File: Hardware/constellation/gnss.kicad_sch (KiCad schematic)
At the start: 0 parts

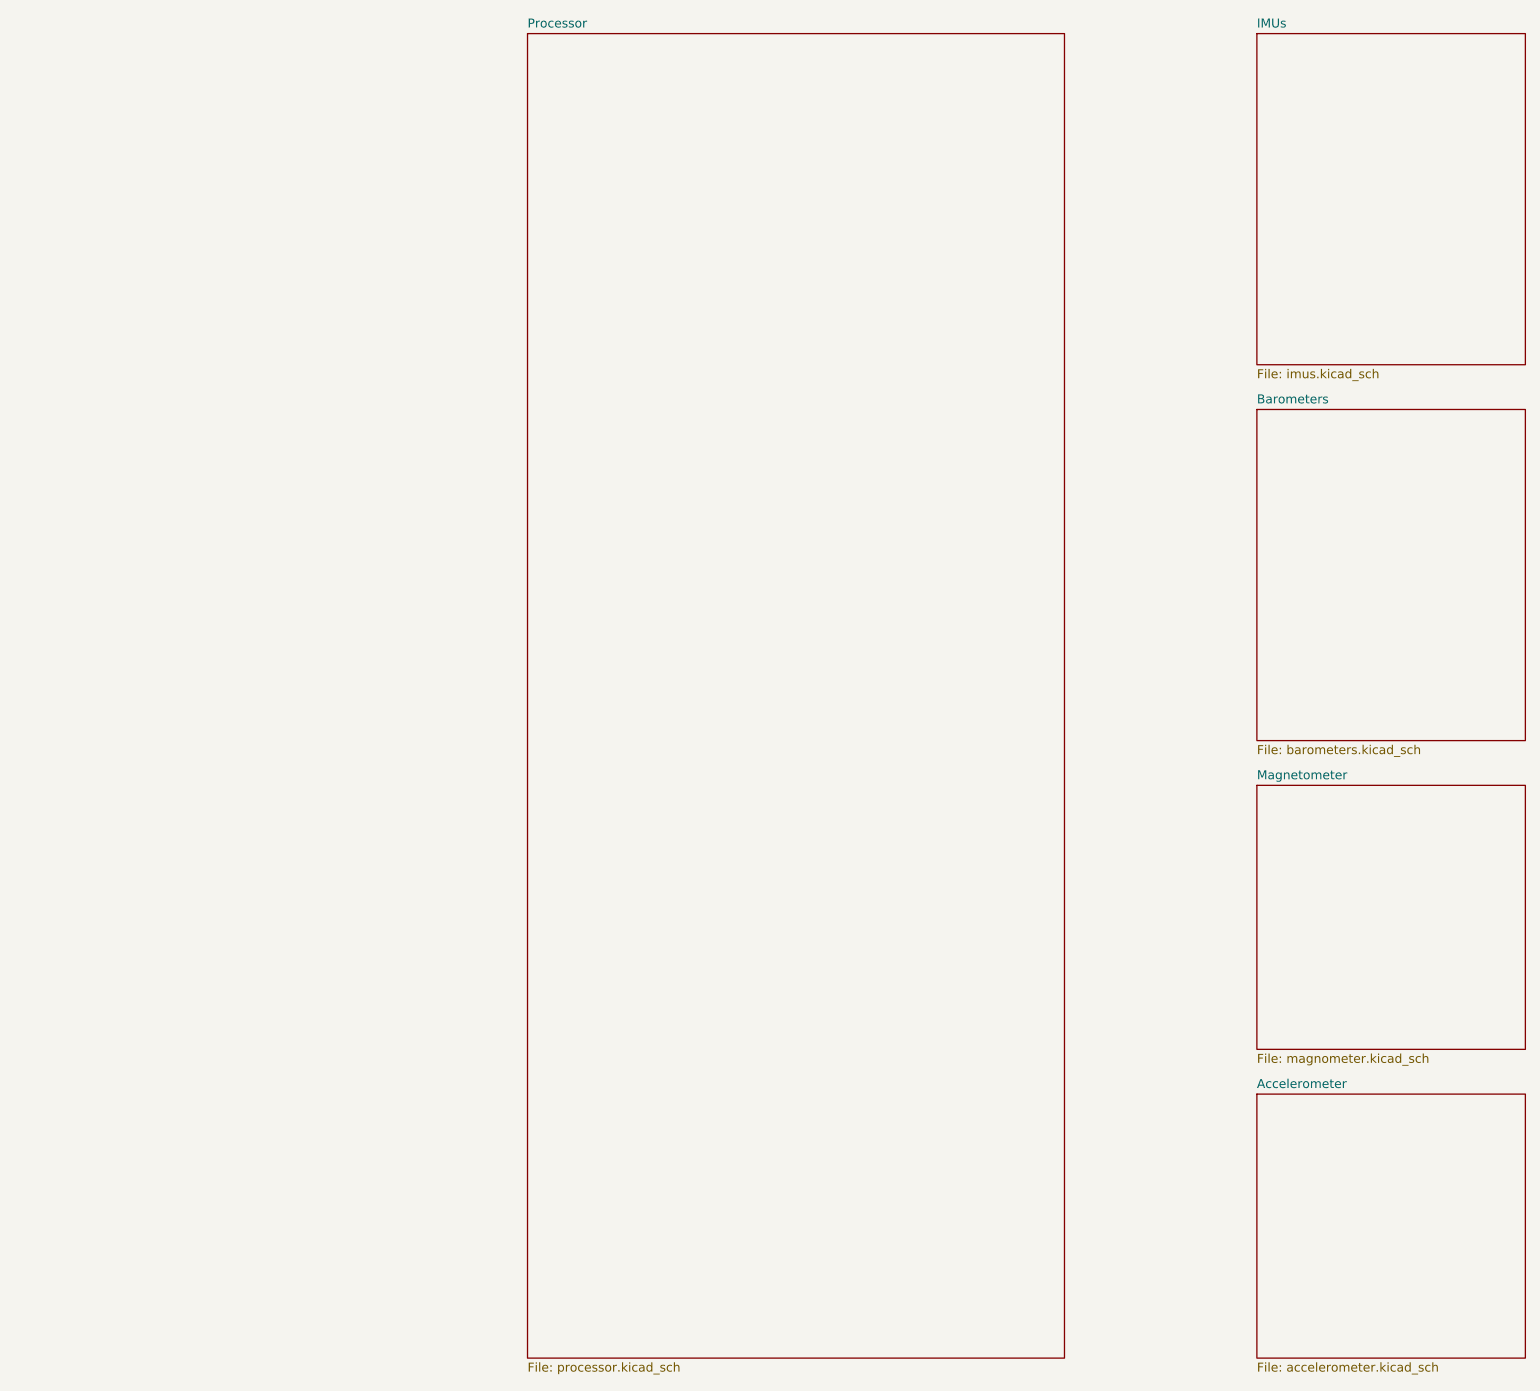
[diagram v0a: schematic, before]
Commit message: shift to hierarchial design, add GNSS, mag, accel
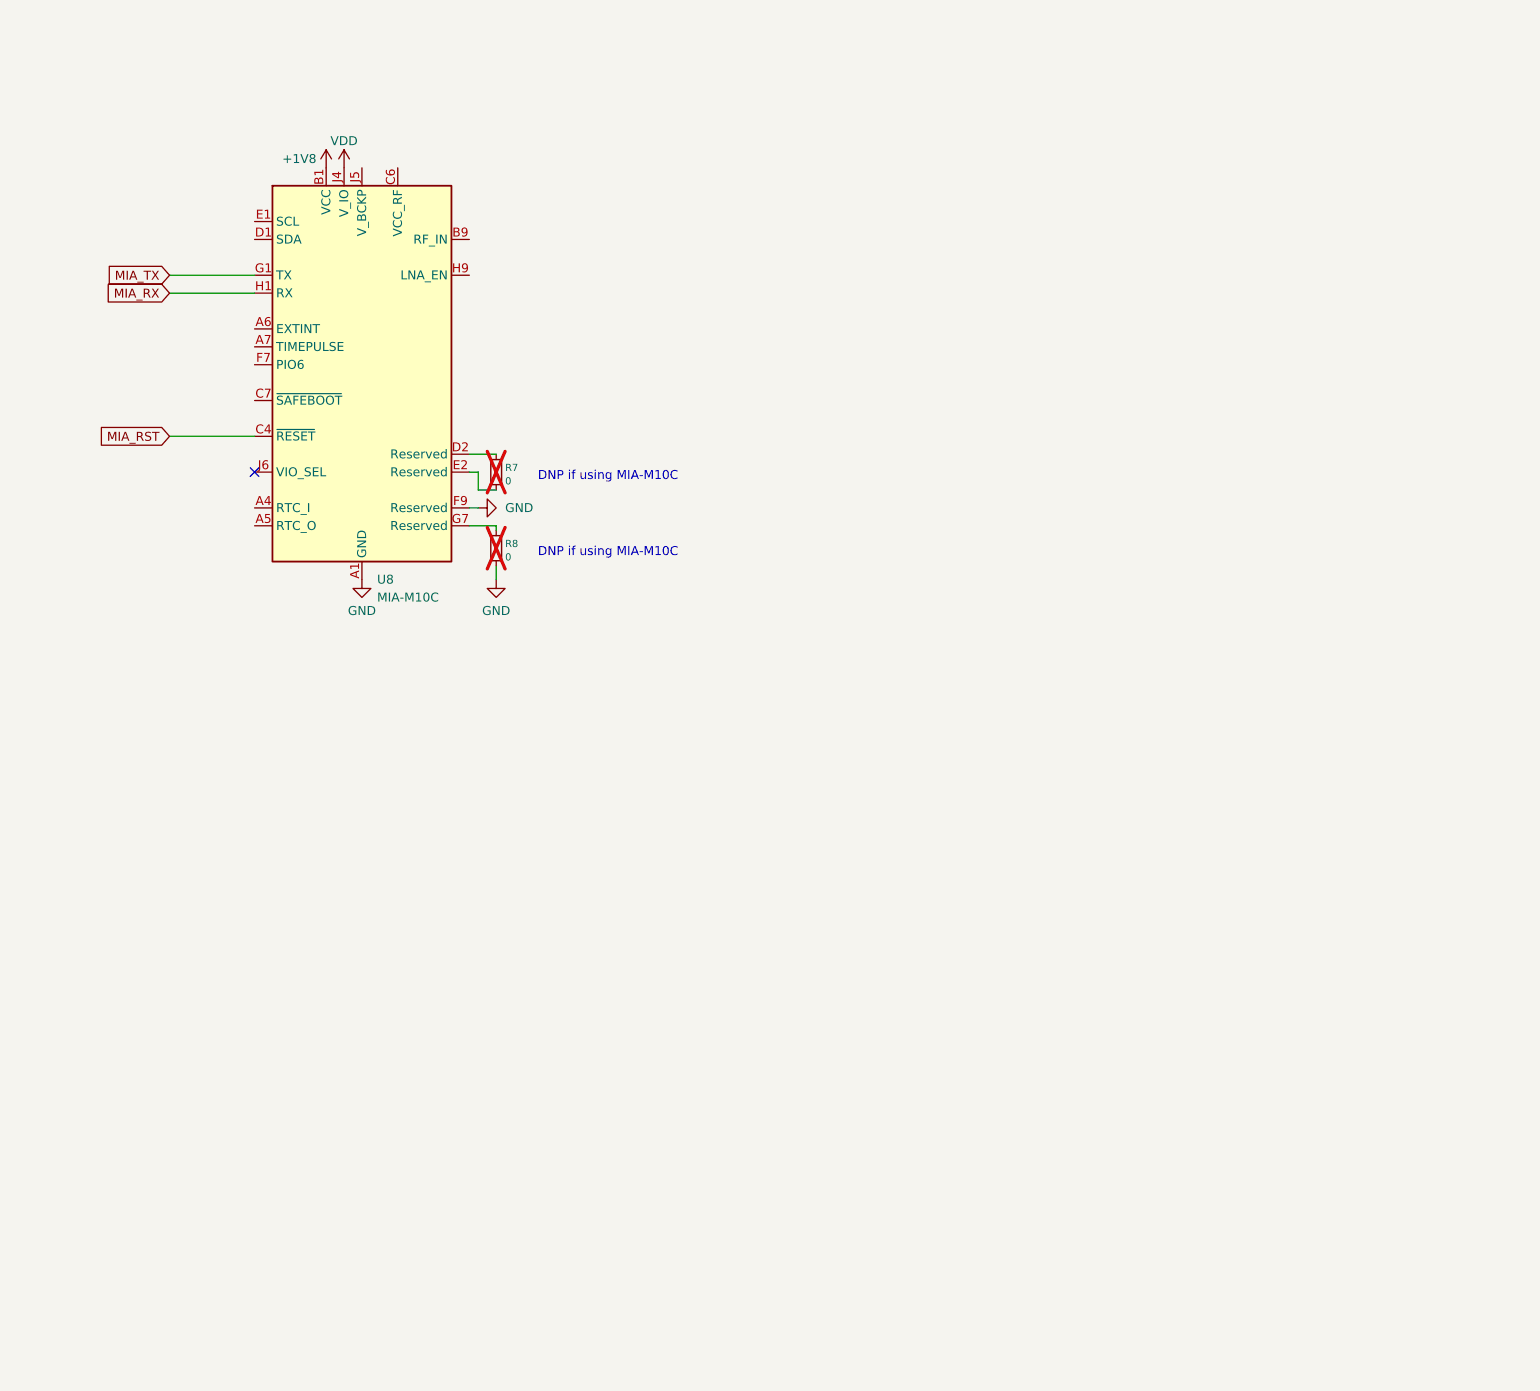
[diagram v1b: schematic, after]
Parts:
- added R7, R8: 0, Resistor_SMD:R_0402_1005Metric_Pad0.72x0.64mm_HandSolder, symbol Device:R_Small
- added U8: MIA-M10C, Package_LGA:ublox_LGA-53_4.5x4.5mm_Layout9x9_P0.5mm, symbol RF_GPS:MIA-M10Q
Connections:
- new net: R7.1, U8.D2 (Reserved)
- new net: R7.2, U8.E2 (Reserved)
- new net: R8.1, U8.G7 (Reserved)
- new net +1V8: U8.B1 (VCC)
- new net GND: R8.2, U8.A1 (GND), U8.A2 (GND), U8.A3 (GND), U8.A8 (GND), U8.A9 (GND), U8.B2 (GND), U8.B8 (GND), U8.C3 (GND), U8.C9 (GND), U8.E3 (GND), U8.E4 (GND), U8.E9 (GND), U8.F1 (GND), U8.F3 (GND), U8.F4 (GND), U8.F9 (Reserved), U8.G3 (GND), U8.G4 (GND), U8.G5 (GND), U8.G6 (GND), U8.H8 (GND), U8.J8 (GND), U8.J9 (GND)
- new net MIA_RST: U8.C4 (~{RESET})
- new net MIA_RX: U8.H1 (RX)
- new net MIA_TX: U8.G1 (TX)
- new net VDD: U8.J4 (V_IO)
- no-connect marks 0 -> 1
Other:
- removed sheet Accelerometer
- removed sheet Barometers
- removed sheet IMUs
- removed sheet Magnetometer
- removed sheet Processor
- note added: "DNP if using MIA-M10C"
- title: Constellation Flight Computer -> GNSS Transceiver Circuitry

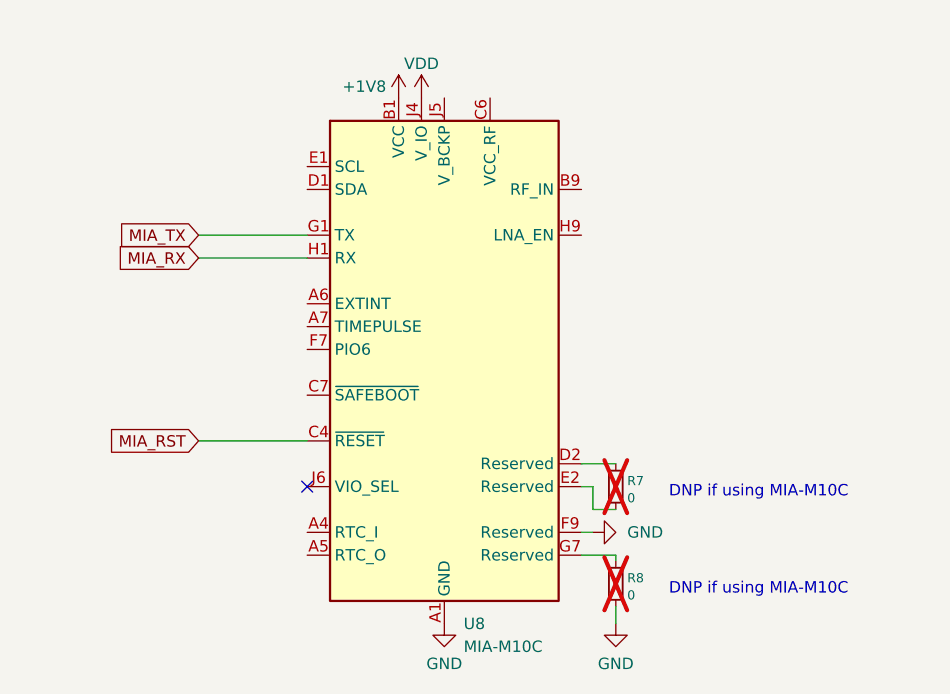
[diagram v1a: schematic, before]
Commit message: add gnss short detection and lna_en supervisor
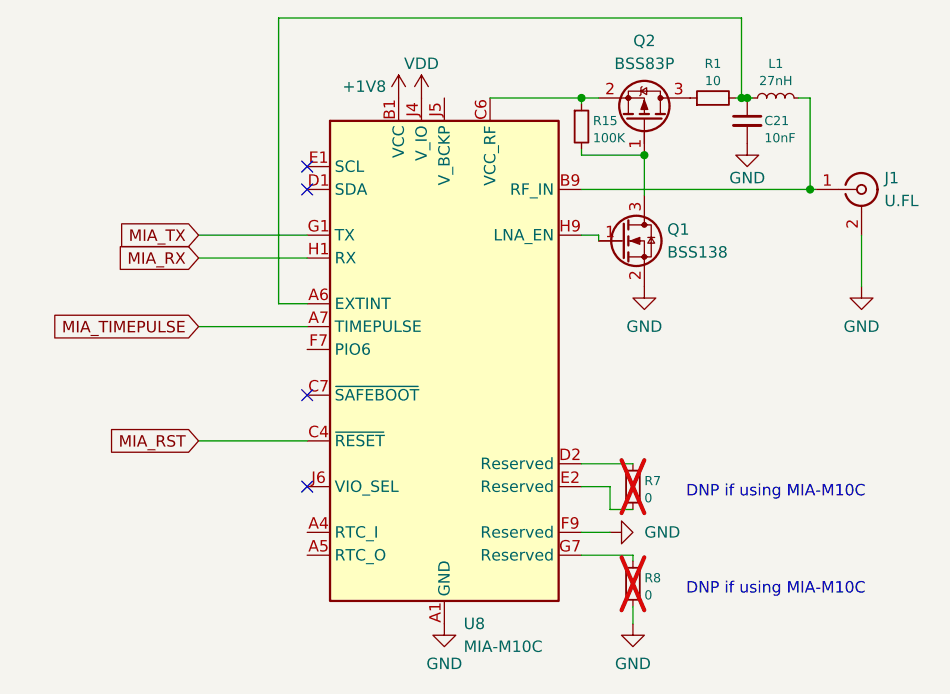
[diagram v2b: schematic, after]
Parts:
- added C21: 10nF, Capacitor_SMD:C_0402_1005Metric, symbol Device:C_Small
- added J1: U.FL, Connector_Coaxial:U.FL_Molex_MCRF_73412-0110_Vertical, symbol Connector:Conn_Coaxial
- added L1: 27nH, Inductor_SMD:L_0402_1005Metric, symbol Device:L_Small
- added Q1: BSS138, Package_TO_SOT_SMD:SOT-23, symbol Transistor_FET:BSS138
- added Q2: BSS83P, Package_TO_SOT_SMD:SOT-23, symbol Transistor_FET:BSS83P
- added R1: 10, Resistor_SMD:R_0402_1005Metric, symbol Device:R_Small
- added R15: 100K, Resistor_SMD:R_0402_1005Metric_Pad0.72x0.64mm_HandSolder, symbol Device:R_Small
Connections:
- net GND: now also C21.2, J1.2 (Ext), Q1.2 (S)
- net at U8.A6 (EXTINT): now also C21.1, L1.1, R1.2
- net MIA_TIMEPULSE: now reaches U8.A7 (TIMEPULSE)
- net at U8.B9 (RF_IN): now also J1.1 (In), L1.2
- net at U8.C6 (VCC_RF): now also Q2.2 (S), R15.1
- net at U8.H9 (LNA_EN): now also Q1.1 (G)
- new net: Q2.3 (D), R1.1
- new net: Q1.3 (D), Q2.1 (G), R15.2
- no-connect marks 1 -> 4
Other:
- moved on the sheet: R7, R8

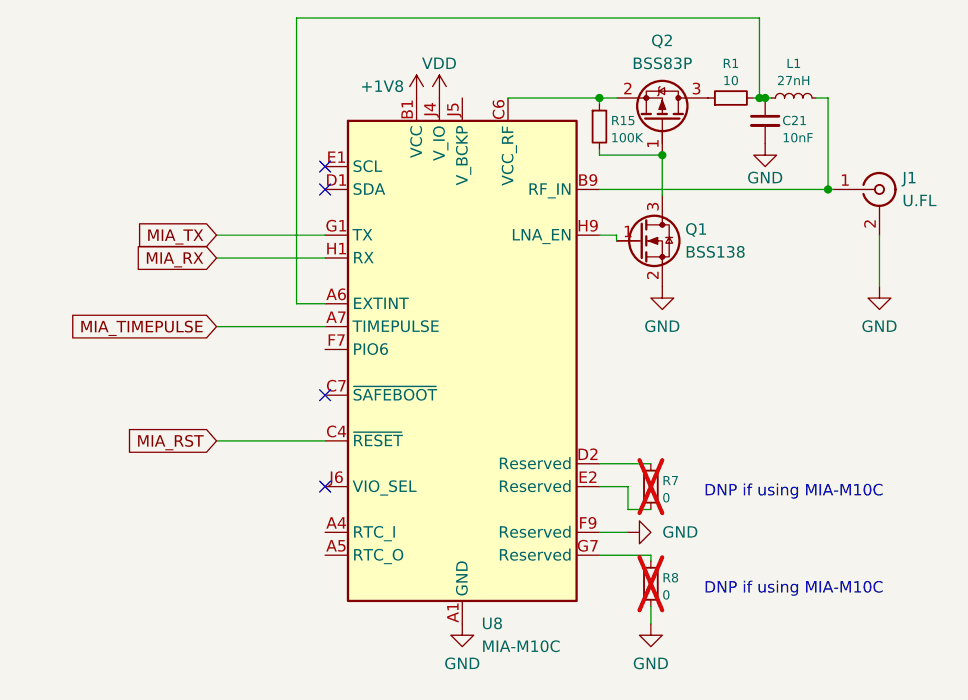
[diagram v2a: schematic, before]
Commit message: convert gnss into hierarchal
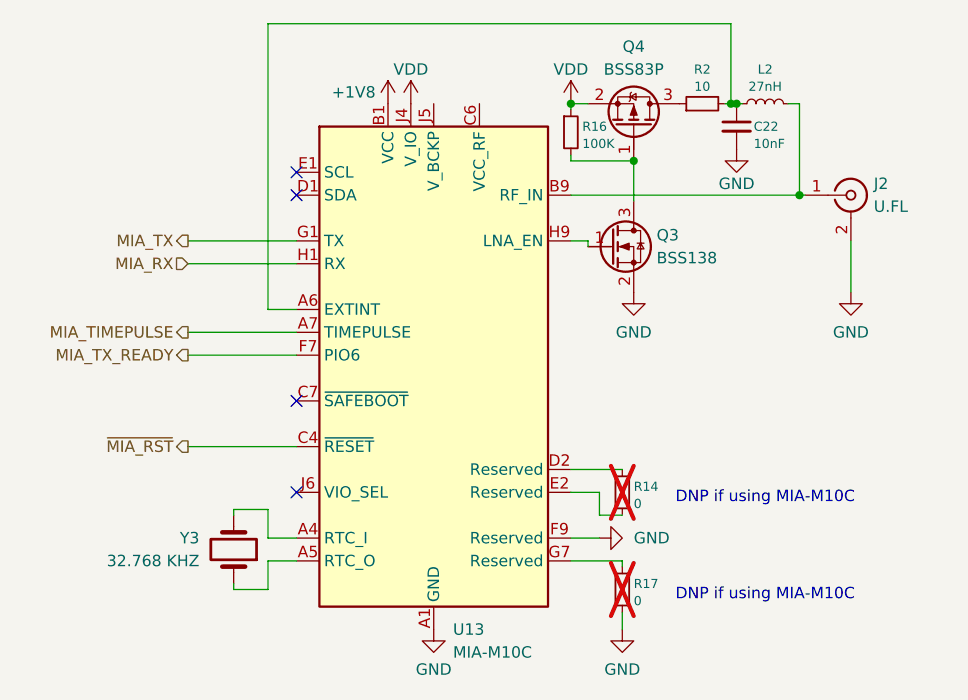
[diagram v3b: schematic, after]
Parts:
- removed C21: 10nF, Capacitor_SMD:C_0402_1005Metric, symbol Device:C_Small
- removed J1: U.FL, Connector_Coaxial:U.FL_Molex_MCRF_73412-0110_Vertical, symbol Connector:Conn_Coaxial
- removed L1: 27nH, Inductor_SMD:L_0402_1005Metric, symbol Device:L_Small
- removed Q1: BSS138, Package_TO_SOT_SMD:SOT-23, symbol Transistor_FET:BSS138
- removed Q2: BSS83P, Package_TO_SOT_SMD:SOT-23, symbol Transistor_FET:BSS83P
- removed R1: 10, Resistor_SMD:R_0402_1005Metric, symbol Device:R_Small
- removed R15: 100K, Resistor_SMD:R_0402_1005Metric_Pad0.72x0.64mm_HandSolder, symbol Device:R_Small
- removed R7, R8: 0, Resistor_SMD:R_0402_1005Metric_Pad0.72x0.64mm_HandSolder, symbol Device:R_Small
- removed U8: MIA-M10C, Package_LGA:ublox_LGA-53_4.5x4.5mm_Layout9x9_P0.5mm, symbol RF_GPS:MIA-M10Q
- added C22: 10nF, Capacitor_SMD:C_0402_1005Metric, symbol Device:C_Small
- added J2: U.FL, Connector_Coaxial:U.FL_Molex_MCRF_73412-0110_Vertical, symbol Connector:Conn_Coaxial
- added L2: 27nH, Inductor_SMD:L_0402_1005Metric, symbol Device:L_Small
- added Q3: BSS138, Package_TO_SOT_SMD:SOT-23, symbol Transistor_FET:BSS138
- added Q4: BSS83P, Package_TO_SOT_SMD:SOT-23, symbol Transistor_FET:BSS83P
- added R14, R17: 0, Resistor_SMD:R_0402_1005Metric_Pad0.72x0.64mm_HandSolder, symbol Device:R_Small
- added R16: 100K, Resistor_SMD:R_0402_1005Metric_Pad0.72x0.64mm_HandSolder, symbol Device:R_Small
- added R2: 10, Resistor_SMD:R_0402_1005Metric, symbol Device:R_Small
- added U13: MIA-M10C, Package_LGA:ublox_LGA-53_4.5x4.5mm_Layout9x9_P0.5mm, symbol RF_GPS:MIA-M10Q
- added Y3: 32.768 KHZ, Crystal:Crystal_SMD_3215-2Pin_3.2x1.5mm, symbol Device:Crystal
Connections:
- net +1V8: now also U13.B1 (VCC)
- net GND: now also C22.2, J2.2 (Ext), Q3.2 (S), R17.2, U13.A1 (GND), U13.A2 (GND), U13.A3 (GND), U13.A8 (GND), U13.A9 (GND), U13.B2 (GND), U13.B8 (GND), U13.C3 (GND), U13.C9 (GND), U13.E3 (GND), U13.E4 (GND), U13.E9 (GND), U13.F1 (GND), U13.F3 (GND), U13.F4 (GND), U13.F9 (Reserved), U13.G3 (GND), U13.G4 (GND), U13.G5 (GND), U13.G6 (GND), U13.H8 (GND), U13.J8 (GND), U13.J9 (GND)
- net MIA_RX: now also U13.H1 (RX)
- net MIA_TIMEPULSE: now also U13.A7 (TIMEPULSE)
- net MIA_TX: now also U13.G1 (TX)
- net VDD: now also Q4.2 (S), R16.1, U13.J4 (V_IO)
- new net: Q4.3 (D), R2.1
- new net: C22.1, L2.1, R2.2, U13.A6 (EXTINT)
- new net: U13.A4 (RTC_I), Y3.2
- new net: U13.A5 (RTC_O), Y3.1
- new net: J2.1 (In), L2.2, U13.B9 (RF_IN)
- new net: R14.1, U13.D2 (Reserved)
- new net: R14.2, U13.E2 (Reserved)
- new net: R17.1, U13.G7 (Reserved)
- new net: Q3.1 (G), U13.H9 (LNA_EN)
- new net: Q3.3 (D), Q4.1 (G), R16.2
- new net MIA_TX_READY: U13.F7 (PIO6)
- new net ~{MIA_RST}: U13.C4 (~{RESET})

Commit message: actually fix the magnetometer issue, start work on lora
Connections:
- no-connect marks 4 -> 5
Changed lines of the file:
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@@
 		(at 130.175 120.015)
+	)
+	(no_connect
+		(at 150.495 76.835)
 	)
 	(wire
@@
 				(path "/ba226b81-7f6b-4f1e-964f-d5311904768c/024ded0e-182d-4822-a380-1069265c1486"
 					(reference "R2")
+					(unit 1)
+				)
+				(path "/ba226b81-7f6b-4f1e-964f-d5311904768c/ee7bb32f-b13d-4ab0-a3c0-7eccf92cdd39"
+					(reference "R3")
 					(unit 1)
 				)
@@
 					(unit 1)
 				)
+				(path "/ba226b81-7f6b-4f1e-964f-d5311904768c/ee7bb32f-b13d-4ab0-a3c0-7eccf92cdd39"
+					(reference "U14")
+					(unit 1)
+				)
 			)
 		)
@@
 					(unit 1)
 				)
+				(path "/ba226b81-7f6b-4f1e-964f-d5311904768c/ee7bb32f-b13d-4ab0-a3c0-7eccf92cdd39"
+					(reference "Q6")
+					(unit 1)
+				)
 			)
 		)
@@
 					(unit 1)
 				)
+				(path "/ba226b81-7f6b-4f1e-964f-d5311904768c/ee7bb32f-b13d-4ab0-a3c0-7eccf92cdd39"
+					(reference "C23")
+					(unit 1)
+				)
 			)
 		)
@@
 				(path "/ba226b81-7f6b-4f1e-964f-d5311904768c/024ded0e-182d-4822-a380-1069265c1486"
 					(reference "#PWR074")
+					(unit 1)
+				)
+				(path "/ba226b81-7f6b-4f1e-964f-d5311904768c/ee7bb32f-b13d-4ab0-a3c0-7eccf92cdd39"
+					(reference "#PWR083")
 					(unit 1)
 				)
@@
 					(unit 1)
 				)
+				(path "/ba226b81-7f6b-4f1e-964f-d5311904768c/ee7bb32f-b13d-4ab0-a3c0-7eccf92cdd39"
+					(reference "#PWR090")
+					(unit 1)
+				)
 			)
 		)
@@
 					(unit 1)
 				)
+				(path "/ba226b81-7f6b-4f1e-964f-d5311904768c/ee7bb32f-b13d-4ab0-a3c0-7eccf92cdd39"
+					(reference "#PWR087")
+					(unit 1)
+				)
 			)
 		)
@@
 				(path "/ba226b81-7f6b-4f1e-964f-d5311904768c/024ded0e-182d-4822-a380-1069265c1486"
 					(reference "Q3")
+					(unit 1)
+				)
+				(path "/ba226b81-7f6b-4f1e-964f-d5311904768c/ee7bb32f-b13d-4ab0-a3c0-7eccf92cdd39"
+					(reference "Q5")
 					(unit 1)
 				)
@@
 					(unit 1)
 				)
+				(path "/ba226b81-7f6b-4f1e-964f-d5311904768c/ee7bb32f-b13d-4ab0-a3c0-7eccf92cdd39"
+					(reference "#PWR084")
+					(unit 1)
+				)
 			)
 		)
@@
 					(unit 1)
 				)
+				(path "/ba226b81-7f6b-4f1e-964f-d5311904768c/ee7bb32f-b13d-4ab0-a3c0-7eccf92cdd39"
+					(reference "#PWR088")
+					(unit 1)
+				)
 			)
 		)
@@
 				(path "/ba226b81-7f6b-4f1e-964f-d5311904768c/024ded0e-182d-4822-a380-1069265c1486"
 					(reference "#PWR076")
+					(unit 1)
+				)
+				(path "/ba226b81-7f6b-4f1e-964f-d5311904768c/ee7bb32f-b13d-4ab0-a3c0-7eccf92cdd39"
+					(reference "#PWR085")
 					(unit 1)
 				)
@@
 					(unit 1)
 				)
+				(path "/ba226b81-7f6b-4f1e-964f-d5311904768c/ee7bb32f-b13d-4ab0-a3c0-7eccf92cdd39"
+					(reference "#PWR086")
+					(unit 1)
+				)
 			)
 		)
@@
 					(unit 1)
 				)
+				(path "/ba226b81-7f6b-4f1e-964f-d5311904768c/ee7bb32f-b13d-4ab0-a3c0-7eccf92cdd39"
+					(reference "R15")
+					(unit 1)
+				)
 			)
 		)
@@
 					(unit 1)
 				)
+				(path "/ba226b81-7f6b-4f1e-964f-d5311904768c/ee7bb32f-b13d-4ab0-a3c0-7eccf92cdd39"
+					(reference "#PWR089")
+					(unit 1)
+				)
 			)
 		)
@@
 					(unit 1)
 				)
+				(path "/ba226b81-7f6b-4f1e-964f-d5311904768c/ee7bb32f-b13d-4ab0-a3c0-7eccf92cdd39"
+					(reference "R19")
+					(unit 1)
+				)
 			)
 		)
@@
 					(unit 1)
 				)
+				(path "/ba226b81-7f6b-4f1e-964f-d5311904768c/ee7bb32f-b13d-4ab0-a3c0-7eccf92cdd39"
+					(reference "L3")
+					(unit 1)
+				)
 			)
 		)
@@
 					(unit 1)
 				)
+				(path "/ba226b81-7f6b-4f1e-964f-d5311904768c/ee7bb32f-b13d-4ab0-a3c0-7eccf92cdd39"
+					(reference "J3")
+					(unit 1)
+				)
 			)
 		)
@@
 					(unit 1)
 				)
+				(path "/ba226b81-7f6b-4f1e-964f-d5311904768c/ee7bb32f-b13d-4ab0-a3c0-7eccf92cdd39"
+					(reference "#PWR082")
+					(unit 1)
+				)
 			)
 		)
@@
 				(path "/ba226b81-7f6b-4f1e-964f-d5311904768c/024ded0e-182d-4822-a380-1069265c1486"
 					(reference "R16")
+					(unit 1)
+				)
+				(path "/ba226b81-7f6b-4f1e-964f-d5311904768c/ee7bb32f-b13d-4ab0-a3c0-7eccf92cdd39"
+					(reference "R18")
 					(unit 1)
 				)
@@
 					(unit 1)
 				)
+				(path "/ba226b81-7f6b-4f1e-964f-d5311904768c/ee7bb32f-b13d-4ab0-a3c0-7eccf92cdd39"
+					(reference "Y4")
+					(unit 1)
+				)
